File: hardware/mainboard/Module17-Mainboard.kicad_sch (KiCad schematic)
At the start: 7 parts

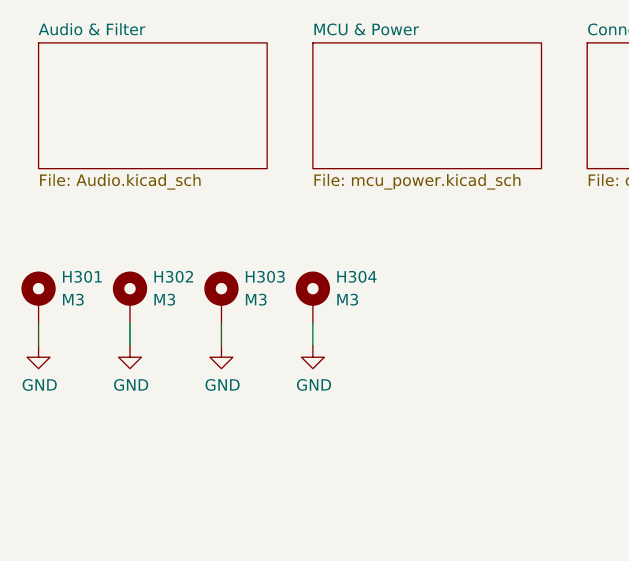
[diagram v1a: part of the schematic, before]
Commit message: Updated mainboard
Replaced OHIS speaker resistors with larger 100 ohms resistors
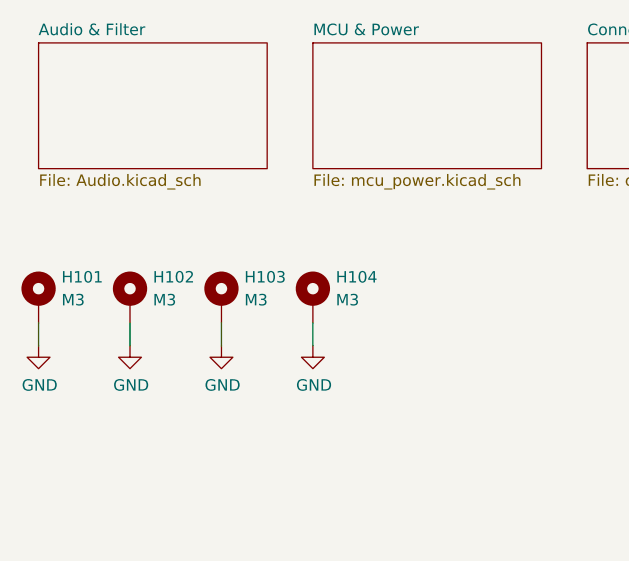
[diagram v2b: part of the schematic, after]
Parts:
- renumbered H301 to H101, H302 to H102, H303 to H103, H304 to H104
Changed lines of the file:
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@@
   (symbol (lib_id "power:GND") (at 25.4 51.435 0) (unit 1)
     (in_bom yes) (on_board yes) (dnp no)
-    (property "Reference" "#PWR0320" (at 25.4 57.785 0)
+    (property "Reference" "#PWR0102" (at 25.4 57.785 0)
       (effects (font (size 1.27 1.27)) hide)
     )
@@
     (instances
       (project "Module17-Mainboard"
-        (path "/59592280-3207-432b-a891-cd517ec5cf12/00000000-0000-0000-0000-0000612c95ef"
-          (reference "#PWR0320") (unit 1)
-        )
         (path "/59592280-3207-432b-a891-cd517ec5cf12"
           (reference "#PWR0102") (unit 1)
@@
   (symbol (lib_id "power:GND") (at 15.24 51.435 0) (unit 1)
     (in_bom yes) (on_board yes) (dnp no)
-    (property "Reference" "#PWR0319" (at 15.24 57.785 0)
+    (property "Reference" "#PWR0101" (at 15.24 57.785 0)
       (effects (font (size 1.27 1.27)) hide)
     )
@@
     (instances
       (project "Module17-Mainboard"
-        (path "/59592280-3207-432b-a891-cd517ec5cf12/00000000-0000-0000-0000-0000612c95ef"
-          (reference "#PWR0319") (unit 1)
-        )
         (path "/59592280-3207-432b-a891-cd517ec5cf12"
           (reference "#PWR0101") (unit 1)
@@
   (symbol (lib_id "Mechanical:MountingHole_Pad") (at 15.24 46.355 0) (unit 1)
     (in_bom no) (on_board yes) (dnp no) (fields_autoplaced)
-    (property "Reference" "H301" (at 17.78 43.815 0)
+    (property "Reference" "H101" (at 17.78 43.815 0)
       (effects (font (size 1.27 1.27)) (justify left))
     )
@@
     (instances
       (project "Module17-Mainboard"
-        (path "/59592280-3207-432b-a891-cd517ec5cf12/00000000-0000-0000-0000-0000612c95ef"
-          (reference "H301") (unit 1)
-        )
         (path "/59592280-3207-432b-a891-cd517ec5cf12"
           (reference "H101") (unit 1)
@@
   (symbol (lib_id "power:GND") (at 35.56 51.435 0) (unit 1)
     (in_bom yes) (on_board yes) (dnp no)
-    (property "Reference" "#PWR0323" (at 35.56 57.785 0)
+    (property "Reference" "#PWR0103" (at 35.56 57.785 0)
       (effects (font (size 1.27 1.27)) hide)
     )
@@
     (instances
       (project "Module17-Mainboard"
-        (path "/59592280-3207-432b-a891-cd517ec5cf12/00000000-0000-0000-0000-0000612c95ef"
-          (reference "#PWR0323") (unit 1)
-        )
         (path "/59592280-3207-432b-a891-cd517ec5cf12"
           (reference "#PWR0103") (unit 1)
@@
   (symbol (lib_id "Mechanical:MountingHole_Pad") (at 25.4 46.355 0) (unit 1)
     (in_bom no) (on_board yes) (dnp no) (fields_autoplaced)
-    (property "Reference" "H302" (at 27.94 43.815 0)
+    (property "Reference" "H102" (at 27.94 43.815 0)
       (effects (font (size 1.27 1.27)) (justify left))
     )
@@
     (instances
       (project "Module17-Mainboard"
-        (path "/59592280-3207-432b-a891-cd517ec5cf12/00000000-0000-0000-0000-0000612c95ef"
-          (reference "H302") (unit 1)
-        )
         (path "/59592280-3207-432b-a891-cd517ec5cf12"
           (reference "H102") (unit 1)
@@
   (symbol (lib_id "power:GND") (at 45.72 51.435 0) (unit 1)
     (in_bom yes) (on_board yes) (dnp no)
-    (property "Reference" "#PWR0327" (at 45.72 57.785 0)
+    (property "Reference" "#PWR0104" (at 45.72 57.785 0)
       (effects (font (size 1.27 1.27)) hide)
     )
@@
     (instances
       (project "Module17-Mainboard"
-        (path "/59592280-3207-432b-a891-cd517ec5cf12/00000000-0000-0000-0000-0000612c95ef"
-          (reference "#PWR0327") (unit 1)
-        )
         (path "/59592280-3207-432b-a891-cd517ec5cf12"
           (reference "#PWR0104") (unit 1)
@@
   (symbol (lib_id "Mechanical:MountingHole_Pad") (at 35.56 46.355 0) (unit 1)
     (in_bom no) (on_board yes) (dnp no) (fields_autoplaced)
-    (property "Reference" "H303" (at 38.1 43.815 0)
+    (property "Reference" "H103" (at 38.1 43.815 0)
       (effects (font (size 1.27 1.27)) (justify left))
     )
@@
     (instances
       (project "Module17-Mainboard"
-        (path "/59592280-3207-432b-a891-cd517ec5cf12/00000000-0000-0000-0000-0000612c95ef"
-          (reference "H303") (unit 1)
-        )
         (path "/59592280-3207-432b-a891-cd517ec5cf12"
           (reference "H103") (unit 1)
@@
   (symbol (lib_id "Mechanical:MountingHole_Pad") (at 45.72 46.355 0) (unit 1)
     (in_bom no) (on_board yes) (dnp no) (fields_autoplaced)
-    (property "Reference" "H304" (at 48.26 43.815 0)
+    (property "Reference" "H104" (at 48.26 43.815 0)
       (effects (font (size 1.27 1.27)) (justify left))
     )
@@
     (instances
       (project "Module17-Mainboard"
-        (path "/59592280-3207-432b-a891-cd517ec5cf12/00000000-0000-0000-0000-0000612c95ef"
-          (reference "H304") (unit 1)
-        )
         (path "/59592280-3207-432b-a891-cd517ec5cf12"
           (reference "H104") (unit 1)
